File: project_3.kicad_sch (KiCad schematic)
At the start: 46 parts, among them J1 USB_C, J2 Conn_01x06, J3 Conn_02x10_Odd_Even, J4 Conn_02x20_Odd_Even, J5 Conn_02x20_Odd_Even, J6 Conn_02x06_Odd_Even, Q1 Q_PMOSFET, SW1 RESET, SW2 ISP, SW3 Use, U1 LPC2148FBD64, U2 AP2112K-3.3, Y1 12 MHz

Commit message: All Clear
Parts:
- removed C1, C2: 18 pF, Capacitor_SMD:C_0603_1608Metric, symbol Device:C
- removed C10, C12, C4, C6, C7, C8, C9: 100nF, Capacitor_SMD:C_0603_1608Metric, symbol Device:C
- removed C11: 4.7uF, Capacitor_SMD:C_0805_2012Metric, symbol Device:C
- removed C3, C5: 10uF, Capacitor_SMD:C_0805_2012Metric, symbol Device:C
- removed D1: SMBJ5.0A, Diode_SMD:D_SMA, symbol Device:D_TVS
- removed D2, D3, D4, D5: LED, LED_SMD:LED_0603_1608Metric, symbol Device:LED
- removed F1: 500mA, symbol Device:Polyfuse
- removed J1: USB_C, Connector_USB:USB_C_Receptacle_GCT_USB4105-xx-A_16P_TopMnt_Horizontal, symbol Connector:USB_C_Receptacle_USB2.0_16P
- removed J2: Conn_01x06, Connector_PinHeader_2.54mm:PinHeader_1x06_P2.54mm_Vertical, symbol Connector_Generic:Conn_01x06
- removed J3: Conn_02x10_Odd_Even, Connector_PinHeader_2.54mm:PinHeader_2x10_P2.54mm_Vertical, symbol Connector_Generic:Conn_02x10_Odd_Even
- removed J4, J5: Conn_02x20_Odd_Even, Connector_PinHeader_2.54mm:PinHeader_2x20_P2.54mm_Vertical, symbol Connector_Generic:Conn_02x20_Odd_Even
- removed J6: Conn_02x06_Odd_Even, Connector_PinHeader_2.54mm:PinHeader_2x06_P2.54mm_Vertical, symbol Connector_Generic:Conn_02x06_Odd_Even
- removed Q1: Q_PMOSFET, Package_TO_SOT_SMD:TO-252-2, symbol Transistor_FET:Q_PMOS_GSD
- removed R1, R3: 10k, Resistor_SMD:R_0603_1608Metric, symbol Device:R
- removed R10, R11, R7, R8, R9: R, Resistor_SMD:R_0603_1608Metric, symbol Device:R
- removed R12, R13, R14, R15, R4, R5, R6: 1k, Resistor_SMD:R_0603_1608Metric, symbol Device:R
- removed R2: R, symbol Device:R
- removed SW1: RESET, Button_Switch_SMD:SW_SPST_TL3305A, symbol Switch:SW_Push
- removed SW2: ISP, Button_Switch_SMD:SW_SPST_TL3305A, symbol Switch:SW_Push
- removed SW3: Use, Button_Switch_SMD:SW_SPST_TL3305A, symbol Switch:SW_Push
- removed U1: LPC2148FBD64, Package_QFP:LQFP-64_10x10mm_P0.5mm, symbol MCU_NXP_LPC:LPC2148FBD64
- removed U2: AP2112K-3.3, Package_TO_SOT_SMD:SOT-23-5, symbol Regulator_Linear:AP2112K-3.3
- removed Y1: 12 MHz, Crystal:Crystal_SMD_0603-4Pin_6.0x3.5mm, symbol Device:Crystal
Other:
- note removed: "GPIO headers"
- note removed: "JTAG"
- note removed: "MCU decouplind"
- note removed: "Main MCU and Clock"
- note removed: "Power input"
- note removed: "Reset and ISP"
- note removed: "Status LEDs"
- note removed: "USB-to-UART"

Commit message: New Model added
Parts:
- added C10, C12, C13, C4, C6, C7, C8, C9: 100nF, Capacitor_SMD:C_0603_1608Metric, symbol Device:C
- added C11: 4.7µF, Capacitor_SMD:C_0603_1608Metric, symbol Device:C
- added C3, C5: 10µF, Capacitor_SMD:C_0805_2012Metric, symbol Device:C
- added D1: SMBJ5.0A, Diode_SMD:D_SMA, symbol Device:D_TVS
- added F1: 500mA PTC, Fuse:Fuse_1206_3216Metric, symbol Device:Polyfuse
- added FB1: Ferrite bead, Inductor_SMD:L_0603_1608Metric, symbol Device:FerriteBead
- added J1: USB_C_Receptacle_USB2.0_16P, Connector_USB:USB_C_Receptacle_GCT_USB4105-xx-A_16P_TopMnt_Horizontal, symbol Connector:USB_C_Receptacle_USB2.0_16P
- added Q1: AO3401A, Package_TO_SOT_SMD:SOT-23-5, symbol Transistor_FET:Q_PMOS_GSD
- added R1, R2: 5.1kΩ, Resistor_SMD:R_0603_1608Metric, symbol Device:R
- added R3, R4: 33Ω, Resistor_SMD:R_0603_1608Metric, symbol Device:R
- added R5: 100kΩ, Resistor_SMD:R_0603_1608Metric, symbol Device:R
- added U1: LPC2148FBD64, Package_QFP:LQFP-64_10x10mm_P0.5mm, symbol MCU_NXP_LPC:LPC2148FBD64
- added U2: USBLC6-2SC6, Package_TO_SOT_SMD:SOT-23-6, symbol Power_Protection:USBLC6-2SC6
- added U3: AP2112K-3.3, Package_TO_SOT_SMD:SOT-23-5, symbol Regulator_Linear:AP2112K-3.3
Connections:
- new net: J1.A1 (GND), J1.A12 (GND), J1.B1 (GND), J1.B12 (GND)
- new net: J1.A4 (VBUS), J1.A9 (VBUS), J1.B4 (VBUS), J1.B9 (VBUS)
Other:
- added sheet Block 10 (Block10.kicad_sch)
- added sheet Block 6 (Block6.kicad_sch)
- added sheet Block 7 (Block7.kicad_sch)
- added sheet Block 8 (Block8.kicad_sch)
- added sheet Block 9 (Block9.kicad_sch)

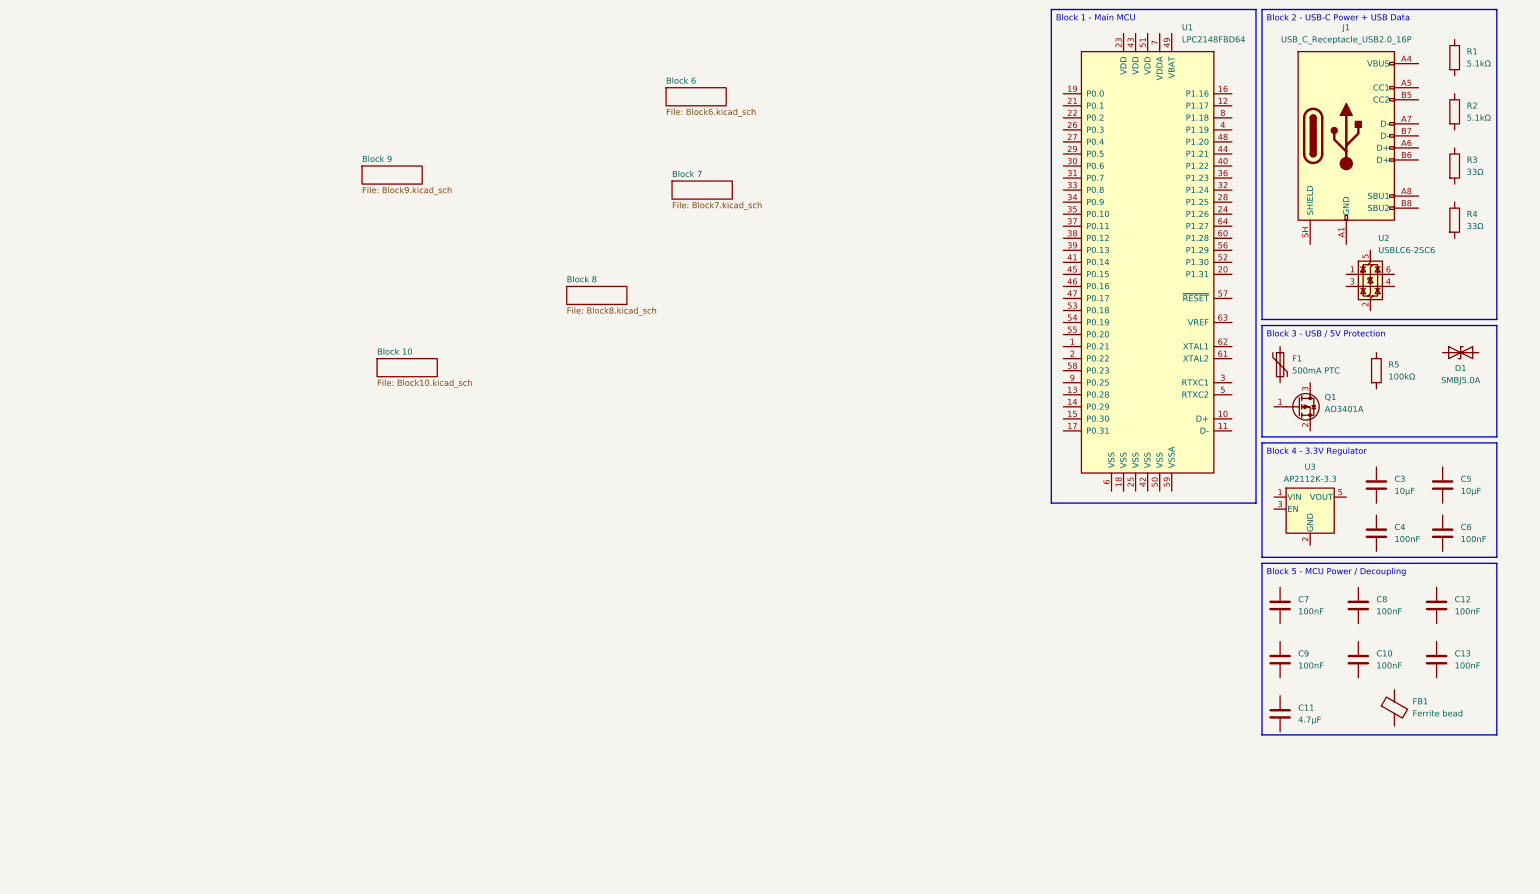
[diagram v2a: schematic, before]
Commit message: Adding NXP modules
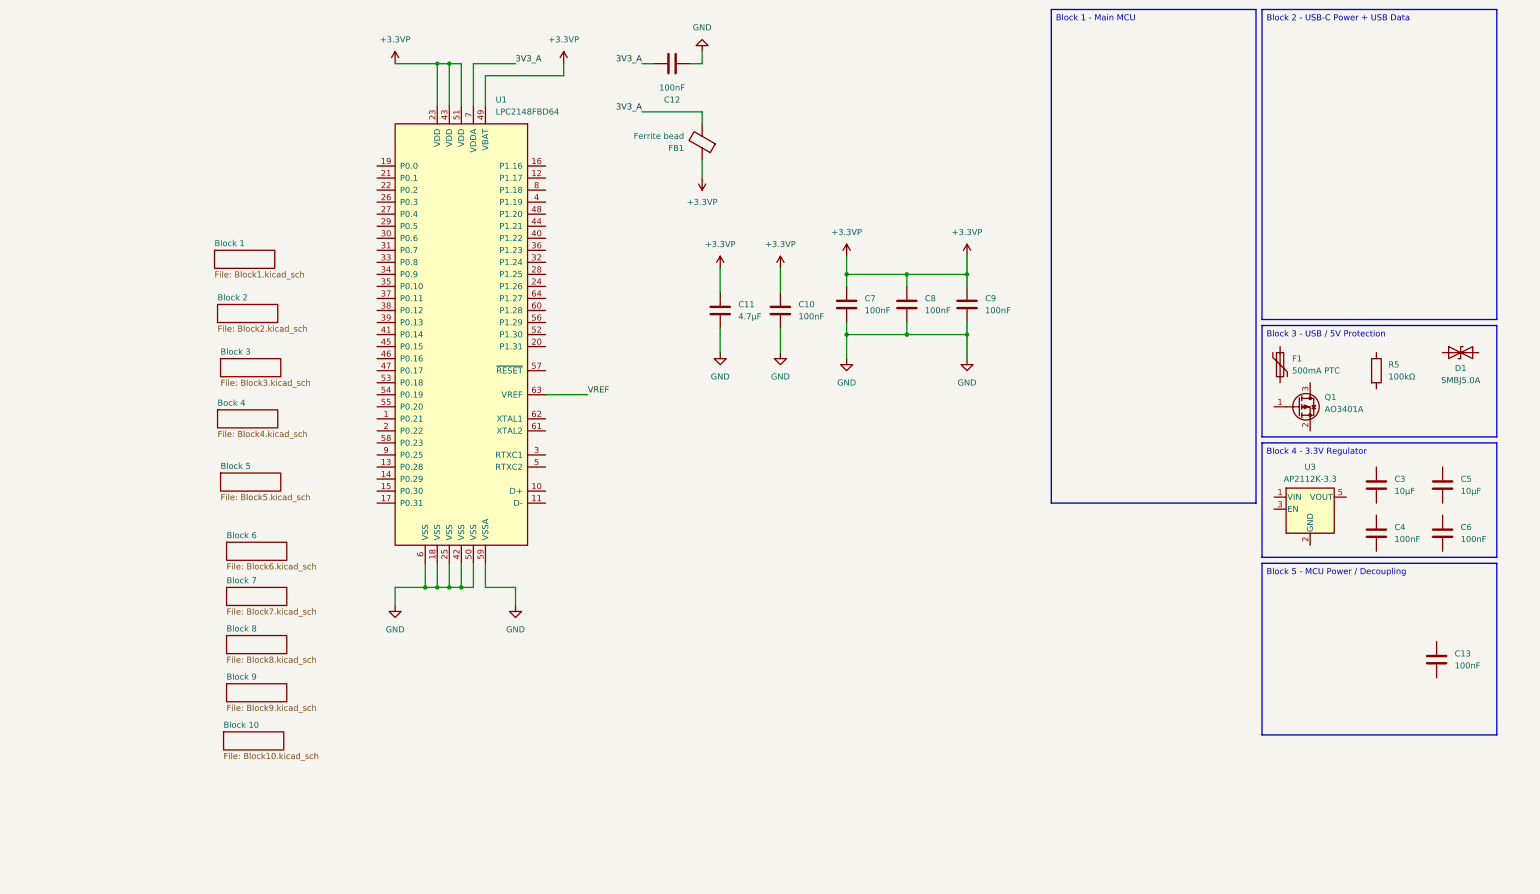
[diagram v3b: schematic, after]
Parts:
- removed J1: USB_C_Receptacle_USB2.0_16P, Connector_USB:USB_C_Receptacle_GCT_USB4105-xx-A_16P_TopMnt_Horizontal, symbol Connector:USB_C_Receptacle_USB2.0_16P
- removed R1, R2: 5.1kΩ, Resistor_SMD:R_0603_1608Metric, symbol Device:R
- removed R3, R4: 33Ω, Resistor_SMD:R_0603_1608Metric, symbol Device:R
- removed U2: USBLC6-2SC6, Package_TO_SOT_SMD:SOT-23-6, symbol Power_Protection:USBLC6-2SC6
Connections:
- net +3.3VP: now reaches C10.1
- net +3.3VP: now also C11.1, C7.1, C8.1, C9.1, FB1.1, U1.23 (VDD), U1.43 (VDD), U1.49 (VBAT), U1.51 (VDD)
- net GND: now reaches C10.2
- net GND: now also C11.2, C12.1, C7.2, C8.2, C9.2, U1.18 (VSS), U1.25 (VSS), U1.42 (VSS), U1.50 (VSS), U1.59 (VSSA), U1.6 (VSS)
- net 3V3_A: now reaches C12.2
- net 3V3_A: now also FB1.2, U1.7 (VDDA)
- net VREF: now reaches U1.63 (VREF)
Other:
- added sheet Block 1 (Block1.kicad_sch)
- added sheet Block 2 (Block2.kicad_sch)
- added sheet Block 3 (Block3.kicad_sch)
- added sheet Block 5 (Block5.kicad_sch)
- added sheet Bock 4 (Block4.kicad_sch)
- moved on the sheet: C12, FB1

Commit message: Usb and ^Power Block added
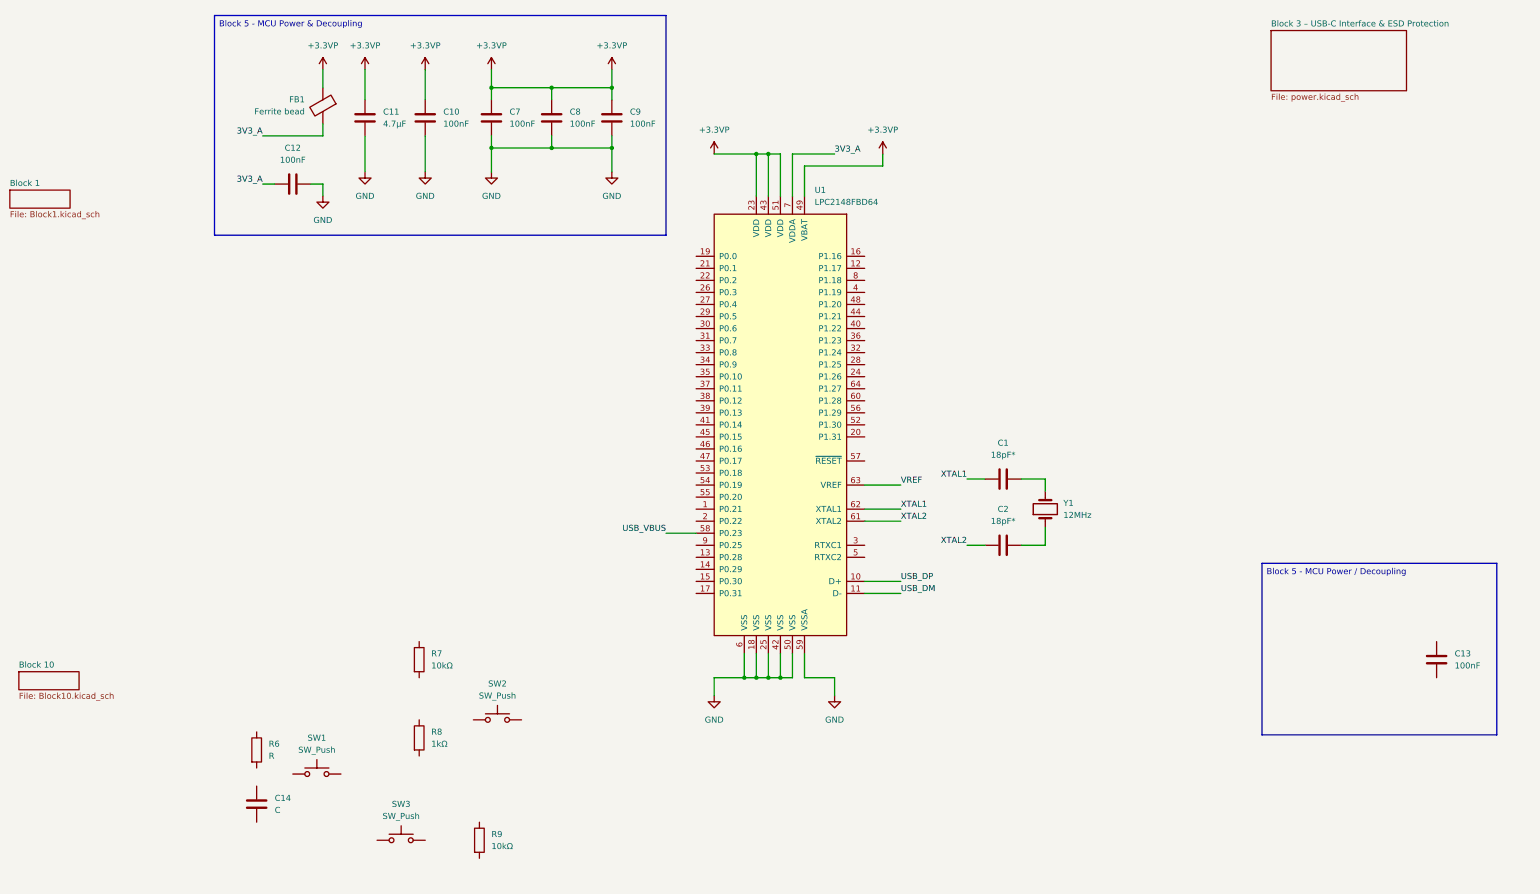
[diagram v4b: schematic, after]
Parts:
- removed C3, C5: 10µF, Capacitor_SMD:C_0805_2012Metric, symbol Device:C
- removed C4, C6: 100nF, Capacitor_SMD:C_0603_1608Metric, symbol Device:C
- removed D1: SMBJ5.0A, Diode_SMD:D_SMA, symbol Device:D_TVS
- removed F1: 500mA PTC, Fuse:Fuse_1206_3216Metric, symbol Device:Polyfuse
- removed Q1: AO3401A, Package_TO_SOT_SMD:SOT-23-5, symbol Transistor_FET:Q_PMOS_GSD
- removed R5: 100kΩ, Resistor_SMD:R_0603_1608Metric, symbol Device:R
- removed U3: AP2112K-3.3, Package_TO_SOT_SMD:SOT-23-5, symbol Regulator_Linear:AP2112K-3.3
- added C1, C2: 18pF*, Resistor_SMD:R_0603_1608Metric, symbol Device:C
- added C14: C, Capacitor_SMD:C_0603_1608Metric, symbol Device:C
- added R6: R, Resistor_SMD:R_0603_1608Metric, symbol Device:R
- added R7, R9: 10kΩ, Resistor_SMD:R_0603_1608Metric, symbol Device:R
- added R8: 1kΩ, Resistor_SMD:R_0603_1608Metric, symbol Device:R
- added SW1, SW2, SW3: SW_Push, Button_Switch_SMD:SW_SPST_TL3305A, symbol Switch:SW_Push
- added Y1: 12MHz, Crystal:Crystal_SMD_3225-4Pin_3.2x2.5mm, symbol Device:Crystal
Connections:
- net USB_DP: now reaches U1.10 (D+)
- net USB_DM: now reaches U1.11 (D-)
- net USB_VBUS: now reaches U1.58 (P0.23)
- net XTAL2: now reaches U1.61 (XTAL2)
- net XTAL2: now also C2.1
- net XTAL1: now reaches U1.62 (XTAL1)
- net XTAL1: now also C1.1
- new net: C1.2, Y1.2
- new net: C2.2, Y1.1
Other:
- removed sheet Block 2
- removed sheet Block 3
- removed sheet Block 5
- removed sheet Block 6
- removed sheet Block 7
- removed sheet Block 8
- removed sheet Block 9
- removed sheet Bock 4
- added sheet Block 3 – USB-C Interface & ESD Protection (power.kicad_sch)

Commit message: ports added
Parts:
- removed C13: 100nF, Capacitor_SMD:C_0603_1608Metric, symbol Device:C
- removed C14: C, Capacitor_SMD:C_0603_1608Metric, symbol Device:C
- added C16: 100nF, Capacitor_SMD:C_0603_1608Metric, symbol Device:C
- added J2: Conn_01x06, Connector_PinHeader_2.54mm:PinHeader_1x06_P2.54mm_Vertical, symbol Connector_Generic:Conn_01x06
- added RN1: 47Ω, Resistor_THT:R_Array_SIP14, symbol Device:R_Pack05
- R6: value R -> 10kΩ
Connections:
- net +3.3VP: now also R6.1, R7.1
- net GND: now also SW1.1, SW2.2, C16.2, J2.2 (Pin_2)
- net P0.21: now reaches U1.1 (P0.21)
- net P0.28: now reaches U1.13 (P0.28)
- net P0.29: now reaches U1.14 (P0.29)
- net P0.30: now reaches U1.15 (P0.30)
- net P0.31: now reaches U1.17 (P0.31)
- net P0.0: now reaches U1.19 (P0.0)
- net P0.0: now also J2.3 (Pin_3)
- net P0.22: now reaches U1.2 (P0.22)
- net at U1.20 (P1.31): now also RN1.10 (R1.2)
- net P0.1: now reaches U1.21 (P0.1)
- net P0.1: now also J2.4 (Pin_4)
- net P0.2: now reaches U1.22 (P0.2)
- net JTAG_RTCK: now reaches U1.24 (P1.26)
- net P0.3: now reaches U1.26 (P0.3)
- net P0.4: now reaches U1.27 (P0.4)
- net P0.5: now reaches U1.29 (P0.5)
- net P0.6: now reaches U1.30 (P0.6)
- net P0.7: now reaches U1.31 (P0.7)
- net P0.8: now reaches U1.33 (P0.8)
- net P0.9: now reaches U1.34 (P0.9)
- net P0.10: now reaches U1.35 (P0.10)
- net P0.11: now reaches U1.37 (P0.11)
- net P0.12: now reaches U1.38 (P0.12)
- net P0.13: now reaches U1.39 (P0.13)
- net ISP_P0_14: now reaches U1.41 (P0.14)
- net ISP_P0_14: now also R7.2, SW2.1, J2.6 (Pin_6)
- net P0.15: now reaches U1.45 (P0.15)
- net P0.16: now reaches U1.46 (P0.16)
- net P0.17: now reaches U1.47 (P0.17)
- net at U1.52 (P1.30): now also RN1.9 (R2.2)
- net P0.18: now reaches U1.53 (P0.18)
- net P0.19: now reaches U1.54 (P0.19)
- net P0.20: now reaches U1.55 (P0.20)
- net at U1.56 (P1.29): now also RN1.8 (R3.2)
- net RESET_N: now reaches U1.57 (~{RESET})
- net RESET_N: now also R6.2, SW1.2, C16.1, J2.5 (Pin_5)
- net at U1.60 (P1.28): now also RN1.7 (R4.2)
- net at U1.64 (P1.27): now also RN1.6 (R5.2)
- net P0.25: now reaches U1.9 (P0.25)
- net USB_VBUS renamed P0.23
- new net 3.3V: J2.1 (Pin_1)
- new net JTAG_TCK: RN1.3 (R3.1)
- new net JTAG_TDI: RN1.4 (R4.1)
- new net JTAG_TDO: RN1.5 (R5.1)
- new net JTAG_TMS: RN1.2 (R2.1)
- new net JTAG_TRST: RN1.1 (R1.1)
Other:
- moved on the sheet: C1, C10, C11, C12, C2, C7, C8, C9, FB1, R6, R7, R8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

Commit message: Circuit Compleated
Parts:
- removed J2: Conn_01x06, Connector_PinHeader_2.54mm:PinHeader_1x06_P2.54mm_Vertical, symbol Connector_Generic:Conn_01x06
- removed R8: 1kΩ, Resistor_SMD:R_0603_1608Metric, symbol Device:R
- removed R9: 10kΩ, Resistor_SMD:R_0603_1608Metric, symbol Device:R
- removed SW3: SW_Push, Button_Switch_SMD:SW_SPST_TL3305A, symbol Switch:SW_Push
- added C3, C5: 10µF, Capacitor_SMD:C_0805_2012Metric, symbol Device:C
- added C4, C6: 100nF, Capacitor_SMD:C_0603_1608Metric, symbol Device:C
- added D1: SMBJ5.0A, Diode_SMD:D_SMA, symbol Device:D_TVS
- added D2, D3, D4, D5: LED, LED_SMD:LED_0603_1608Metric, symbol Device:LED
- added F1: 500mA PTC, Fuse:Fuse_1206_3216Metric, symbol Device:Polyfuse
- added J1: USB_C_Receptacle_USB2.0_16P, Connector_USB:USB_C_Receptacle_GCT_USB4105-xx-A_16P_TopMnt_Horizontal, symbol Connector:USB_C_Receptacle_USB2.0_16P
- added Q1: AO3401A, Package_TO_SOT_SMD:SOT-23-5, symbol Transistor_FET:Q_PMOS_GSD
- added Q2: BC847, Package_TO_SOT_SMD:SOT-23, symbol Transistor_BJT:BC847
- added R1, R2: 5.1kΩ, Resistor_SMD:R_0603_1608Metric, symbol Device:R
- added R10, R11, R12, R13: 1k, Resistor_SMD:R_0603_1608Metric, symbol Device:R
- added R16: 1.5kΩ, Package_TO_SOT_SMD:SOT-23, symbol Device:R
- added R17: 10kΩ, Resistor_SMD:R_0603_1608Metric, symbol Device:R
- added R3, R4: 33Ω, Resistor_SMD:R_0603_1608Metric, symbol Device:R
- added R5: 100kΩ, Resistor_SMD:R_0603_1608Metric, symbol Device:R
- added U2: USBLC6-2SC6, Package_TO_SOT_SMD:SOT-23-6, symbol Power_Protection:USBLC6-2SC6
- added U3: AP2112K-3.3, Package_TO_SOT_SMD:SOT-23-5, symbol Regulator_Linear:AP2112K-3.3
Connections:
- net GND: now also C3.2, C4.2, C5.2, C6.2, D1.1 (A1), J1.A1 (GND), J1.A12 (GND), J1.B1 (GND), J1.B12 (GND), J1.SH (SHIELD), R1.2, R10.2, R2.2, R5.2, U2.2 (GND), U3.2 (GND)
- net P0.0: now also R13.2
- net P0.23: now also F1.1, J1.A4 (VBUS), J1.A9 (VBUS), J1.B4 (VBUS), J1.B9 (VBUS), U2.5 (VBUS)
- net P0.31: now also R17.1
- net USB_DM: now also R4.2
- net USB_DP: now also R16.1, R3.2
- net P1.17: now reaches U1.12 (P1.17)
- net P1.16: now reaches U1.16 (P1.16)
- net P1.16: now also R11.2
- net P1.31: now reaches RN1.10 (R1.2), U1.20 (P1.31)
- net P1.25: now reaches U1.28 (P1.25)
- net P1.24: now reaches U1.32 (P1.24)
- net P1.23: now reaches U1.36 (P1.23)
- net P1.19: now reaches U1.4 (P1.19)
- net P1.22: now reaches U1.40 (P1.22)
- net P1.21: now reaches U1.44 (P1.21)
- net P1.20: now reaches U1.48 (P1.20)
- net P1.30: now reaches RN1.9 (R2.2), U1.52 (P1.30)
- net P1.29: now reaches RN1.8 (R3.2), U1.56 (P1.29)
- net P1.28: now reaches RN1.7 (R4.2), U1.60 (P1.28)
- net P1.27: now reaches RN1.6 (R5.2), U1.64 (P1.27)
- net P1.18: now reaches U1.8 (P1.18)
- net +3.3VP renamed +3.3V
- net +3.3V: now also C5.1, C6.1, D2.1 (K), D3.1 (K), D4.1 (K), D5.1 (K), Q2.3 (C), U3.5 (VOUT)
- net P0.10 renamed AD1.2
- net P0.12 renamed AD1.3
- net P0.13 renamed AD1.4
- net P0.15 renamed AD1.5
- net P0.21 renamed AD1.6
- net P0.22 renamed AD1.7
- net P0.25 renamed AD0.4
- net P0.28 renamed AD0.1
- net P0.29 renamed AD0.2
- net P0.30 renamed AD0.3
- net P0.4 renamed AD0.6
- net P0.5 renamed AD0.7
- net P0.6 renamed AD1.0
- net P0.8 renamed AD1.1
- new net: Q1.1 (G), R5.1
- new net: D4.2 (A), R12.1
- new net: J1.B5 (CC2), R2.1
- new net: R4.1, U2.4 (I/O2)
- new net: Q2.1 (B), R17.2
- new net: D5.2 (A), R13.1
- new net: R3.1, U2.6 (I/O1)
- new net: D2.2 (A), R10.1
- new net: J1.A5 (CC1), R1.1
- new net: J1.A6 (D+), J1.B6 (D+), U2.1 (I/O1)
- new net: J1.A7 (D-), J1.B7 (D-), U2.3 (I/O2)
- new net: Q2.2 (E), R16.2
- new net: D3.2 (A), R11.1
- new net +5V_PROTECTED: C3.1, C4.1, Q1.3 (D), U3.1 (VIN), U3.3 (EN)
- new net USB_5V_FUSED: D1.2 (A2), F1.2, Q1.2 (S)
- new net USB_CONNECT: R12.2
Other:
- removed sheet Block 1
- removed sheet Block 3 – USB-C Interface & ESD Protection
- moved on the sheet: C10, C11, C12, C16, C7, C8, C9, FB1, R6, R7, SW1, SW2

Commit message: Upgraded
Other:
- title: (none) -> Arm Header Pinout Board
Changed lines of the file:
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@@
 	(paper "A4")
 	(title_block
+		(title "Arm Header Pinout Board")
 		(rev "0.1v")
 		(company "Devendra Kashyap")
